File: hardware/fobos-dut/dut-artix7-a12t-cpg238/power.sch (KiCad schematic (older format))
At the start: 72 parts, among them J3 575-8, J4 Glitch, J5 Conn_01x02, J6 Measure, J8 575-8, J9 Measure, Q1 FDS9435A, Q2 MBT3904DW1, Q3 BSS138, SW2 SW_DIP_x03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

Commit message: Connected the fixed signals to the FPGA, flexible IO are left unconnected Added 0.1 ohm resistors to the 1V8 and 3V3 power rails, added test points which allow for easy measurement Updated ARTIX7-A12T-CPG238 symbol to make schematic route similarly to the last symbol Connected CFGVBS signal to the 3V3 rail, was previously connected to VCCINT which was a mistake Ran through 7 Series schematic review checklist - 7_Series_Schematic_Review_Recommendations.xlsm Added Xilinx pinout files for the CPG238 package Generated schematic for the csg325 for easy referencing
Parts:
- added R75, R76: 0.1R, Resistor_SMD:R_0805_2012Metric_Pad1.20x1.40mm_HandSolder, symbol Device:R
- added TP10, TP11, TP8, TP9: 5281, cerg:5281, symbol cerg:5281
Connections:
- wire segments 252 -> 261
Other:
- note added: "DNP"
- moved on the sheet: R41, R42, R49, R50, S1, TP5, TP6, TP7

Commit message: Added SMA-JOHNSON-142-0701-201 Vertical SMA footprint to CERG lib, added this footprint to the Vcore measurement Re-positioned Power circuitry to the top right quadrant Re-positioned FOBOS connector to the center on the left edge of the board Re-positioned JTAG Connector, Mode switch, and gain control switch to the top left quadrant of the board
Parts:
- D1: symbol dk_LED-Indication-Discrete:LG_L29K-G2J1-24-Z -> device:LED
- J6: footprint cerg:SMA-JOHNSON-142-0701-801 -> cerg:SMA-JOHNSON-142-0701-201
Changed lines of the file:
@@
 F 0 "J6" H 9250 2650 50  0000 L CNN
 F 1 "Measure" H 9050 2550 50  0000 L CNN
-F 2 "cerg:SMA-JOHNSON-142-0701-801" H 9450 2600 50  0001 C CNN
+F 2 "cerg:SMA-JOHNSON-142-0701-201" H 9450 2600 50  0001 C CNN
 F 3 "~" H 9450 2600 50  0001 C CNN
 F 4 "CONN SMA JACK STR 50OHM EDGE MNT" H 9450 2650 50  0001 C CNN "Description"
@@
 $EndComp
 $Comp
-L dk_LED-Indication-Discrete:LG_L29K-G2J1-24-Z D1
+L device:LED D1
 U 1 1 5FE31482
-P 8550 5100
-F 0 "D1" V 8447 5278 60  0000 L CNN
-F 1 "LG_L29K-G2J1-24-Z" V 8553 5278 60  0001 L CNN
-F 2 "LED_SMD:LED_0603_1608Metric" H 8750 5300 60  0001 L CNN
-F 3 "https://dammedia.osram.info/media/resource/hires/osram-dam-2493945/LG%20L29K.pdf" H 8750 5400 60  0001 L CNN
-F 4 "475-2709-1-ND" H 8750 5500 60  0001 L CNN "Digi-Key_PN"
-F 5 "LG L29K-G2J1-24-Z" H 8750 5600 60  0001 L CNN "MPN"
-F 6 "Optoelectronics" H 8750 5700 60  0001 L CNN "Category"
-F 7 "LED Indication - Discrete" H 8750 5800 60  0001 L CNN "Family"
-F 8 "https://dammedia.osram.info/media/resource/hires/osram-dam-2493945/LG%20L29K.pdf" H 8750 5900 60  0001 L CNN "DK_Datasheet_Link"
-F 9 "/product-detail/en/osram-opto-semiconductors-inc/LG-L29K-G2J1-24-Z/475-2709-1-ND/1938876" H 8750 6000 60  0001 L CNN "DK_Detail_Page"
-F 10 "LED GREEN DIFFUSED 0603 SMD" H 8750 6100 60  0001 L CNN "Description"
-F 11 "OSRAM Opto Semiconductors Inc." H 8750 6200 60  0001 L CNN "Manufacturer"
-F 12 "Active" H 8750 6300 60  0001 L CNN "Status"
-	1    8550 5100
-	0    1    1    0
+P 8550 5050
+F 0 "D1" V 8447 5228 60  0000 L CNN
+F 1 "LG_L29K-G2J1-24-Z" V 8553 5228 60  0001 L CNN
+F 2 "LED_SMD:LED_0603_1608Metric" H 8750 5250 60  0001 L CNN
+F 3 "https://dammedia.osram.info/media/resource/hires/osram-dam-2493945/LG%20L29K.pdf" H 8750 5350 60  0001 L CNN
+F 4 "475-2709-1-ND" H 8750 5450 60  0001 L CNN "Digi-Key_PN"
+F 5 "LG L29K-G2J1-24-Z" H 8750 5550 60  0001 L CNN "MPN"
+F 6 "Optoelectronics" H 8750 5650 60  0001 L CNN "Category"
+F 7 "LED Indication - Discrete" H 8750 5750 60  0001 L CNN "Family"
+F 8 "https://dammedia.osram.info/media/resource/hires/osram-dam-2493945/LG%20L29K.pdf" H 8750 5850 60  0001 L CNN "DK_Datasheet_Link"
+F 9 "/product-detail/en/osram-opto-semiconductors-inc/LG-L29K-G2J1-24-Z/475-2709-1-ND/1938876" H 8750 5950 60  0001 L CNN "DK_Detail_Page"
+F 10 "LED GREEN DIFFUSED 0603 SMD" H 8750 6050 60  0001 L CNN "Description"
+F 11 "OSRAM Opto Semiconductors Inc." H 8750 6150 60  0001 L CNN "Manufacturer"
+F 12 "Active" H 8750 6250 60  0001 L CNN "Status"
+	1    8550 5050
+	0    -1   -1   0
 $EndComp
 $Comp

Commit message: updated library ref for diode and FET, placed target connector and some parts
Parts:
- D1: symbol device:LED -> Device:LED
- Q3: symbol Transistor:BSS138 -> Transistor_FET:BSS138
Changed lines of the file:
@@
 $EndComp
 $Comp
-L device:LED D1
+L Device:LED D1
 U 1 1 5FE31482
 P 8550 5050
@@
 	1750 1250 2000 1250
 $Comp
-L Transistor:BSS138 Q3
+L Transistor_FET:BSS138 Q3
 U 1 1 60AC196A
 P 8450 5900

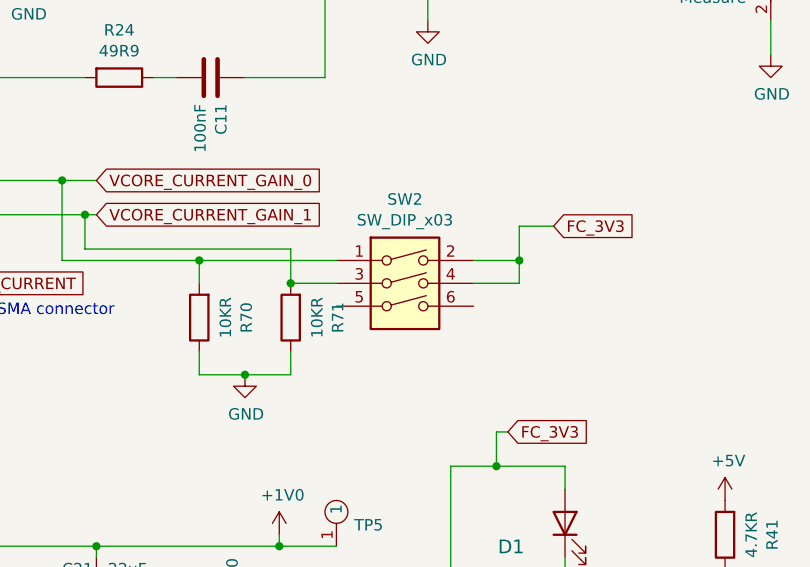
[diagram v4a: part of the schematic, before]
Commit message: moved power jumpers and added graphic
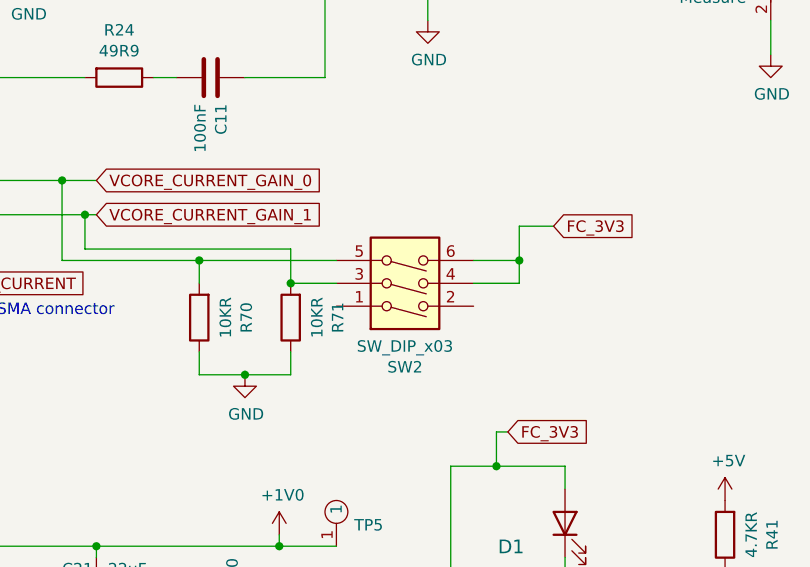
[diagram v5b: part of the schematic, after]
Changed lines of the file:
@@
 L cerg:SW_DIP_x03 SW2
 U 1 1 604378F8
-P 7850 4100
-F 0 "SW2" H 7850 4567 50  0000 C CNN
-F 1 "SW_DIP_x03" H 7850 4476 50  0000 C CNN
-F 2 "cerg:DS04-254-2-03BK-SMT" H 7850 4100 50  0001 C CNN
-F 3 "https://www.cuidevices.com/product/resource/ds04-254-smt.pdf" H 7850 4100 50  0001 C CNN
-F 4 "DS04-254-2-03BK-SMT" H 7850 4475 50  0001 C CNN "MPN"
-F 5 "DIP SWITCH, SPST, 2.54 PITCH, FL" H 7850 4100 50  0001 C CNN "Description"
-F 6 "CUI Devices" H 7850 4100 50  0001 C CNN "Manufacturer"
-	1    7850 4100
-	1    0    0    -1
+P 7850 3900
+F 0 "SW2" H 7850 4367 50  0000 C CNN
+F 1 "SW_DIP_x03" H 7850 4276 50  0000 C CNN
+F 2 "cerg:DS04-254-2-03BK-SMT" H 7850 3900 50  0001 C CNN
+F 3 "https://www.cuidevices.com/product/resource/ds04-254-smt.pdf" H 7850 3900 50  0001 C CNN
+F 4 "DS04-254-2-03BK-SMT" H 7850 4275 50  0001 C CNN "MPN"
+F 5 "DIP SWITCH, SPST, 2.54 PITCH, FL" H 7850 3900 50  0001 C CNN "Description"
+F 6 "CUI Devices" H 7850 3900 50  0001 C CNN "Manufacturer"
+	1    7850 3900
+	1    0    0    1
 $EndComp
 Wire Wire Line

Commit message: modified BJT in power circuit to match ordered BOM
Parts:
- removed Q2: MBT3904DW1, Package_TO_SOT_SMD:SOT-363_SC-70-6, symbol Transistor_BJT:MBT3904DW1
- added Q2, Q8: MMBT3904, Package_TO_SOT_SMD:SOT-23, symbol Transistor_BJT:MMBT3904
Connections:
- net labels added: EN2, EN3, FB1, FB2, FB3, MODE, SW1, SW2, SW3, pre1V8, pre3V3
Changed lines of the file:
@@
 	1450 6350 1450 6400
-$Comp
-L Transistor_BJT:MBT3904DW1 Q2
-U 1 1 5FE4035B
-P 2250 7250
-F 0 "Q2" H 2440 7296 50  0000 L CNN
-F 1 "MBT3904DW1" H 2440 7205 50  0000 L CNN
-F 2 "Package_TO_SOT_SMD:SOT-363_SC-70-6" H 2450 7350 50  0001 C CNN
-F 3 "http://www.onsemi.com/pub_link/Collateral/MBT3904DW1T1-D.PDF" H 2250 7250 50  0001 C CNN
-F 4 "TRANS 2NPN 40V 0.2A SC88" H 2250 7250 50  0001 C CNN "Description"
-F 5 "MBT3904DW1T1G" H 2250 7250 50  0001 C CNN "MPN"
-F 6 "ON Semiconductor" H 2250 7250 50  0001 C CNN "Manufacturer"
-	1    2250 7250
-	1    0    0    -1
-$EndComp
-$Comp
-L Transistor_BJT:MBT3904DW1 Q2
-U 2 1 5FE416AF
-P 1700 7500
-F 0 "Q2" H 1890 7546 50  0000 L CNN
-F 1 "MBT3904DW1" H 1890 7455 50  0000 L CNN
-F 2 "Package_TO_SOT_SMD:SOT-363_SC-70-6" H 1900 7600 50  0001 C CNN
-F 3 "http://www.onsemi.com/pub_link/Collateral/MBT3904DW1T1-D.PDF" H 1700 7500 50  0001 C CNN
-F 4 "TRANS 2NPN 40V 0.2A SC88" H 1700 7500 50  0001 C CNN "Description"
-F 5 "MBT3904DW1T1G" H 1700 7500 50  0001 C CNN "MPN"
-F 6 "ON Semiconductor" H 1700 7500 50  0001 C CNN "Manufacturer"
-	2    1700 7500
-	1    0    0    -1
-$EndComp
 $Comp
 L Device:R R40
@@
 Wire Wire Line
 	7300 5650 7100 5650
+$Comp
+L Transistor_BJT:MMBT3904 Q2
+U 1 1 60C2A20E
+P 1700 7500
+F 0 "Q2" H 1891 7546 50  0000 L CNN
+F 1 "MMBT3904" H 1891 7455 50  0000 L CNN
+F 2 "Package_TO_SOT_SMD:SOT-23" H 1900 7425 50  0001 L CIN
+F 3 "https://www.onsemi.com/pub/Collateral/2N3903-D.PDF" H 1700 7500 50  0001 L CNN
+	1    1700 7500
+	1    0    0    -1
+$EndComp
+$Comp
+L Transistor_BJT:MMBT3904 Q8
+U 1 1 60C2BF42
+P 2250 7250
+F 0 "Q8" H 2441 7296 50  0000 L CNN
+F 1 "MMBT3904" H 2441 7205 50  0000 L CNN
+F 2 "Package_TO_SOT_SMD:SOT-23" H 2450 7175 50  0001 L CIN
+F 3 "https://www.onsemi.com/pub/Collateral/2N3903-D.PDF" H 2250 7250 50  0001 L CNN
+	1    2250 7250
+	1    0    0    -1
+$EndComp
+Text Label 6100 6150 0    50   ~ 0
+pre3V3
+Text Label 6150 5650 0    50   ~ 0
+pre1V8
+Text Label 2600 5950 0    50   ~ 0
+EN3
+Text Label 2800 6800 0    50   ~ 0
+EN2
+Text Label 2600 6200 0    50   ~ 0
+MODE
+Text Label 4750 5550 0    50   ~ 0
+FB1
+Text Label 4750 6050 0    50   ~ 0
+FB2
+Text Label 4750 6550 0    50   ~ 0
+FB3
+Text Label 4650 5150 0    50   ~ 0
+SW1
+Text Label 4700 5650 0    50   ~ 0
+SW2
+Text Label 4700 6150 0    50   ~ 0
+SW3
 $EndSCHEMATC

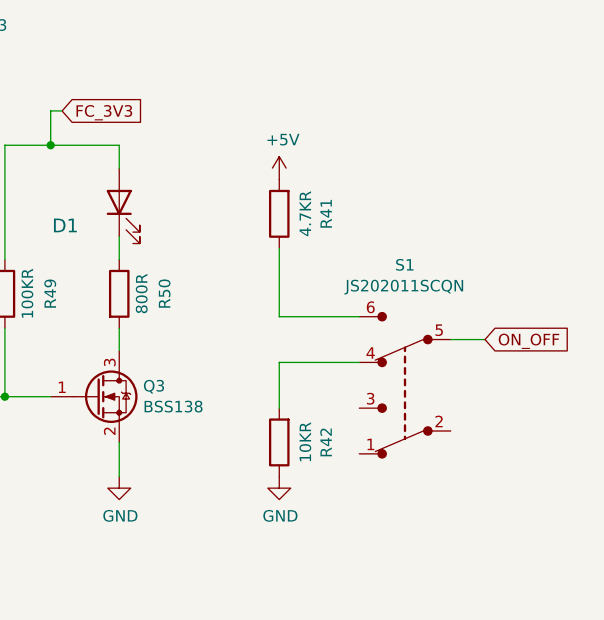
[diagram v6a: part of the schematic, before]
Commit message: everything placed on top except decoupling caps
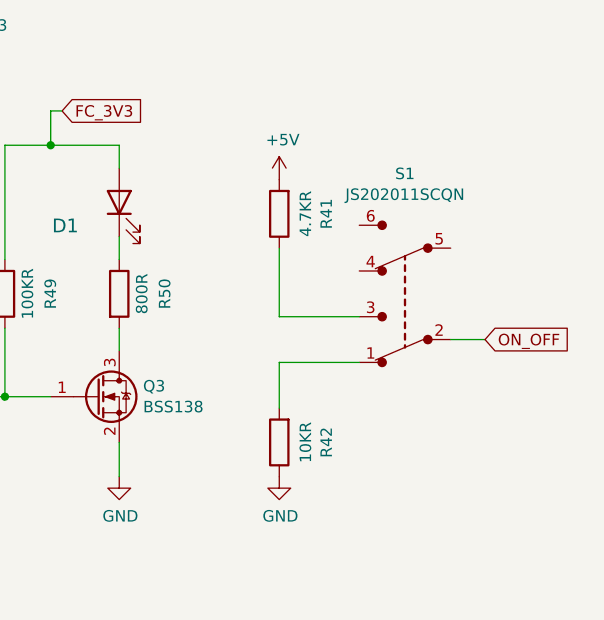
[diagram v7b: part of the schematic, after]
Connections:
- net ON_OFF: now also S1.2; no longer S1.5
- net at R42.2: now also S1.1; no longer S1.4
- net at R41.1: now also S1.3; no longer S1.6
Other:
- moved on the sheet: S1
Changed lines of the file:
@@
 L cerg:JS202011SCQN S1
 U 1 1 60AFF5C6
-P 9800 5850
-F 0 "S1" H 9800 5325 50  0000 C CNN
-F 1 "JS202011SCQN" H 9800 5416 50  0000 C CNN
-F 2 "cerg:Switch_Slide_JS202011SCQN" H 10000 6050 50  0001 L CNN
-F 3 "https://www.ckswitches.com/media/1422/js.pdf" H 10000 6150 60  0001 L CNN
-F 4 "401-2002-1-ND" H 10000 6250 60  0001 L CNN "Digi-Key_PN"
-F 5 "JS202011SCQN" H 10000 6350 60  0001 L CNN "MPN"
-F 6 "Switches" H 10000 6450 60  0001 L CNN "Category"
-F 7 "Slide Switches" H 10000 6550 60  0001 L CNN "Family"
-F 8 "https://www.ckswitches.com/media/1422/js.pdf" H 10000 6650 60  0001 L CNN "DK_Datasheet_Link"
-F 9 "/product-detail/en/c-k/JS202011SCQN/401-2002-1-ND/1640098" H 10000 6750 60  0001 L CNN "DK_Detail_Page"
-F 10 "SWITCH SLIDE DPDT 300MA 6V" H 10000 6850 60  0001 L CNN "Description"
-F 11 "C&K" H 10000 6950 60  0001 L CNN "Manufacturer"
-F 12 "Active" H 10000 7050 60  0001 L CNN "Status"
-	1    9800 5850
+P 9800 5450
+F 0 "S1" H 9800 4925 50  0000 C CNN
+F 1 "JS202011SCQN" H 9800 5016 50  0000 C CNN
+F 2 "cerg:Switch_Slide_JS202011SCQN" H 10000 5650 50  0001 L CNN
+F 3 "https://www.ckswitches.com/media/1422/js.pdf" H 10000 5750 60  0001 L CNN
+F 4 "401-2002-1-ND" H 10000 5850 60  0001 L CNN "Digi-Key_PN"
+F 5 "JS202011SCQN" H 10000 5950 60  0001 L CNN "MPN"
+F 6 "Switches" H 10000 6050 60  0001 L CNN "Category"
+F 7 "Slide Switches" H 10000 6150 60  0001 L CNN "Family"
+F 8 "https://www.ckswitches.com/media/1422/js.pdf" H 10000 6250 60  0001 L CNN "DK_Datasheet_Link"
+F 9 "/product-detail/en/c-k/JS202011SCQN/401-2002-1-ND/1640098" H 10000 6350 60  0001 L CNN "DK_Detail_Page"
+F 10 "SWITCH SLIDE DPDT 300MA 6V" H 10000 6450 60  0001 L CNN "Description"
+F 11 "C&K" H 10000 6550 60  0001 L CNN "Manufacturer"
+F 12 "Active" H 10000 6650 60  0001 L CNN "Status"
+	1    9800 5450
 	-1   0    0    1
 $EndComp

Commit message: swapped location of measurement and glitch SMA and many other little changes
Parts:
- removed JP5: Conn_01x02, Connector_PinHeader_2.54mm:PinHeader_1x02_P2.54mm_Vertical, symbol Connector_Generic:Conn_01x02
- removed TP6, TP7: 5281, cerg:5281, symbol cerg:5281
- J4: footprint cerg:SMA-JOHNSON-142-0701-801 -> cerg:SMA-JOHNSON-142-0701-201
- J6: footprint cerg:SMA-JOHNSON-142-0701-201 -> cerg:SMA-JOHNSON-142-0701-801
- renumbered TP10 to TP6, TP11 to TP7
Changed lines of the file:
@@
 F 0 "J4" H 6288 2296 50  0000 L CNN
 F 1 "Glitch" H 6288 2205 50  0000 L CNN
-F 2 "cerg:SMA-JOHNSON-142-0701-801" H 6200 2250 50  0001 C CNN
+F 2 "cerg:SMA-JOHNSON-142-0701-201" H 6200 2250 50  0001 C CNN
 F 3 "~" H 6200 2250 50  0001 C CNN
 F 4 "CONN SMA JACK STR 50OHM EDGE MNT" H 6200 2300 50  0001 C CNN "Description"
@@
 F 0 "J6" H 9250 2650 50  0000 L CNN
 F 1 "Measure" H 9050 2550 50  0000 L CNN
-F 2 "cerg:SMA-JOHNSON-142-0701-201" H 9450 2600 50  0001 C CNN
+F 2 "cerg:SMA-JOHNSON-142-0701-801" H 9450 2600 50  0001 C CNN
 F 3 "~" H 9450 2600 50  0001 C CNN
 F 4 "CONN SMA JACK STR 50OHM EDGE MNT" H 9450 2650 50  0001 C CNN "Description"
@@
 Wire Wire Line
 	6200 1900 6200 2200
-Wire Wire Line
-	6200 1900 6300 1900
 Connection ~ 6200 1900
 Text Notes 3450 950  0    79   ~ 0
@@
 	4450 1900 4350 1900
 Wire Wire Line
-	6400 1700 6300 1700
-Wire Wire Line
-	6300 1700 6300 1900
-Connection ~ 6300 1900
-$Comp
-L Connector_Generic:Conn_01x02 JP5
-U 1 1 5F45A276
-P 6600 1700
-F 0 "JP5" H 6519 1375 50  0000 C CNN
-F 1 "Conn_01x02" H 6519 1466 50  0000 C CNN
-F 2 "Connector_PinHeader_2.54mm:PinHeader_1x02_P2.54mm_Vertical" H 6600 1700 50  0001 C CNN
-F 3 "~" H 6600 1700 50  0001 C CNN
-F 4 "CONN HEADER VERT 2POS 2.54MM" H 6600 1700 50  0001 C CNN "Description"
-F 5 "10129378-902001BLF" H 6600 1700 50  0001 C CNN "MPN"
-F 6 "Amphenol ICC (FCI)" H 6600 1700 50  0001 C CNN "Manufacturer"
-	1    6600 1700
-	1    0    0    1
-$EndComp
-$Comp
-L power:GND #PWR?
-U 1 1 5F45A27C
-P 6150 1600
-AR Path="/5B6DA40D/5F45A27C" Ref="#PWR?"  Part="1"
-AR Path="/5B6C87CC/5F45A27C" Ref="#PWR?"  Part="1"
-AR Path="/5BE3725D/5F45A27C" Ref="#PWR?"  Part="1"
-AR Path="/5F227C5D/5F45A27C" Ref="#PWR?"  Part="1"
-AR Path="/5F449901/5F45A27C" Ref="#PWR0115"  Part="1"
-F 0 "#PWR0115" H 6150 1350 50  0001 C CNN
-F 1 "GND" H 6155 1427 50  0000 C CNN
-F 2 "" H 6150 1600 50  0001 C CNN
-F 3 "" H 6150 1600 50  0001 C CNN
-	1    6150 1600
-	1    0    0    -1
-$EndComp
-Wire Wire Line
-	6400 1600 6150 1600
-Wire Wire Line
 	5550 1550 5800 1550
 $Comp
@@
 $EndComp
 Wire Wire Line
-	6300 1900 6850 1900
-Wire Wire Line
 	3000 2800 3000 2850
 Wire Wire Line
@@
 $EndComp
 $Comp
-L cerg:5281 TP6
-U 1 1 5FFD5035
-P 7550 5550
-F 0 "TP6" H 7628 5542 50  0000 L CNN
-F 1 "5281" H 7628 5497 50  0001 L CNN
-F 2 "cerg:5281" H 7550 5550 50  0001 C CNN
-F 3 "https://www.keyelco.com/product.cfm/product_id/14628/stepAccess/2813779" H 7550 5550 50  0001 C CNN
-F 4 "TEST POINT (BLACK) - MULTIPURPOS" H 7550 5550 50  0001 C CNN "Description"
-F 5 "5281" H 7550 5550 50  0001 C CNN "MPN"
-F 6 "Keystone Electronics" H 7550 5550 50  0001 C CNN "Manufacturer"
-	1    7550 5550
-	1    0    0    -1
-$EndComp
-$Comp
-L cerg:5281 TP7
-U 1 1 5FFD53A8
-P 7550 6050
-F 0 "TP7" V 7545 6178 50  0000 L CNN
-F 1 "5281" V 7590 6178 50  0001 L CNN
-F 2 "cerg:5281" H 7550 6050 50  0001 C CNN
-F 3 "https://www.keyelco.com/product.cfm/product_id/14628/stepAccess/2813779" H 7550 6050 50  0001 C CNN
-F 4 "TEST POINT (BLACK) - MULTIPURPOS" H 7550 6050 50  0001 C CNN "Description"
-F 5 "5281" H 7550 6050 50  0001 C CNN "MPN"
-F 6 "Keystone Electronics" H 7550 6050 50  0001 C CNN "Manufacturer"
-	1    7550 6050
-	1    0    0    -1
-$EndComp
-$Comp
 L cerg:5281 TP1
 U 1 1 6000136A
@@
 $EndComp
 $Comp
-L cerg:5281 TP10
+L cerg:5281 TP6
 U 1 1 60C21AB4
 P 7100 5500
-F 0 "TP10" V 7095 5628 50  0000 L CNN
+F 0 "TP6" V 7095 5628 50  0000 L CNN
 F 1 "5281" V 7140 5628 50  0001 L CNN
 F 2 "cerg:5281" H 7100 5500 50  0001 C CNN
@@
 $EndComp
 $Comp
-L cerg:5281 TP11
+L cerg:5281 TP7
 U 1 1 60C22508
 P 7100 6000
-F 0 "TP11" V 7095 6128 50  0000 L CNN
+F 0 "TP7" V 7095 6128 50  0000 L CNN
 F 1 "5281" V 7140 6128 50  0001 L CNN
 F 2 "cerg:5281" H 7100 6000 50  0001 C CNN
@@
 Wire Wire Line
 	7100 6100 7100 6150
-Wire Wire Line
-	7550 6150 7300 6150
 Connection ~ 7100 6150
 Wire Wire Line
 	7300 6100 7300 6150
-Connection ~ 7300 6150
 Wire Wire Line
 	7300 6150 7100 6150
 Wire Wire Line
-	7550 5650 7300 5650
-Wire Wire Line
 	7100 5600 7100 5650
 Connection ~ 7100 5650
@@
 Wire Wire Line
 	7300 5600 7300 5650
-Connection ~ 7300 5650
 Wire Wire Line
 	7300 5650 7100 5650
@@
 Text Label 4700 6150 0    50   ~ 0
 SW3
+Wire Wire Line
+	6200 1900 6850 1900
 $EndSCHEMATC
